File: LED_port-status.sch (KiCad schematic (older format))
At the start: 25 parts, among them P1 CONN_9

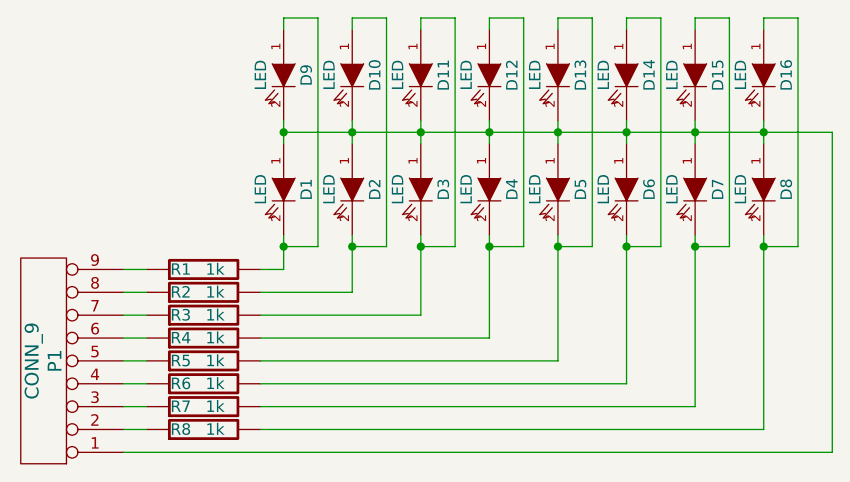
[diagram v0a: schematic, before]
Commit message: Switched to SMD resistor 4-packs.
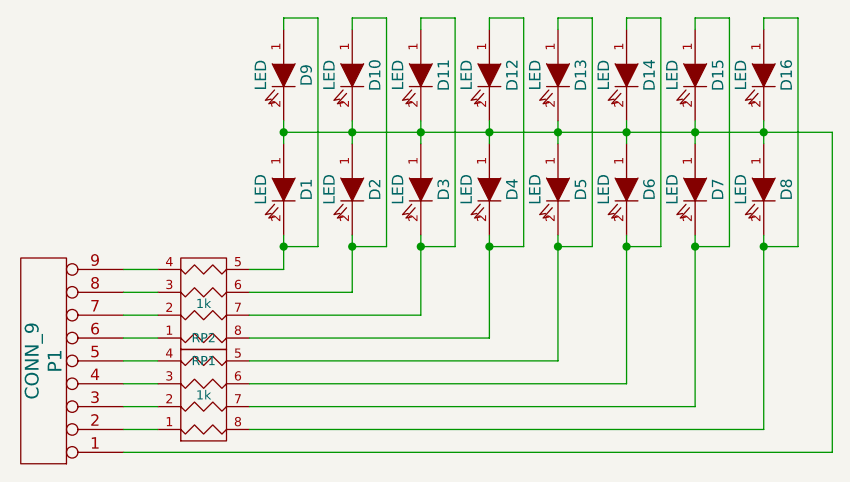
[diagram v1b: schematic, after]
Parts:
- removed R1, R2, R3, R4, R5, R6, R7, R8: 1k, symbol R
- added RP1, RP2: 1k, symbol R_PACK4
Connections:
- net at P1.2 (P2): now also RP2.1 (P1)
- net at P1.3 (P3): now also RP2.2 (P2)
- net at P1.4 (P4): now also RP2.3 (P3)
- net at P1.5 (P5): now also RP2.4 (P4)
- net at P1.6 (P6): now also RP1.1 (P1)
- net at P1.7 (P7): now also RP1.2 (P2)
- net at P1.8 (P8): now also RP1.3 (P3)
- net at P1.9 (P9): now also RP1.4 (P4)
- net at D1.2 (K), D9.1 (A): now also RP1.5 (R4)
- net at D10.1 (A), D2.2 (K): now also RP1.6 (R3)
- net at D11.1 (A), D3.2 (K): now also RP1.7 (R2)
- net at D12.1 (A), D4.2 (K): now also RP1.8 (R1)
- net at D13.1 (A), D5.2 (K): now also RP2.5 (R4)
- net at D14.1 (A), D6.2 (K): now also RP2.6 (R3)
- net at D15.1 (A), D7.2 (K): now also RP2.7 (R2)
- net at D16.1 (A), D8.2 (K): now also RP2.8 (R1)
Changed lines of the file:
@@
-EESchema Schematic File Version 2  date Mon 10 Dec 2012 09:48:04 PM CET
+EESchema Schematic File Version 2  date Sun 17 Feb 2013 02:52:17 PM CET
 LIBS:power
 LIBS:device
@@
 LIBS:contrib
 LIBS:valves
+LIBS:my_parts
 LIBS:LED_port-status-cache
 EELAYER 27 0
@@
 Sheet 1 1
 Title "LED_port-status"
-Date "10 dec 2012"
-Rev "0.10"
+Date "17 feb 2013"
+Rev "0.2"
 Comp "2012 - blog.spitzenpfeil.org"
 Comment1 ""
@@
 F 0 "P1" V 2150 3100 60  0000 C CNN
 F 1 "CONN_9" V 2250 3100 60  0000 C CNN
+F 2 "" H 2200 3100 60  0001 C CNN
+F 3 "" H 2200 3100 60  0001 C CNN
 	1    2200 3100
 	-1   0    0    1
-$EndComp
-$Comp
-L R R1
-U 1 1 50C62340
-P 2900 2700
-F 0 "R1" V 2900 2800 50  0000 C CNN
-F 1 "1k" V 2900 2650 50  0000 C CNN
-	1    2900 2700
-	0    -1   -1   0
-$EndComp
-$Comp
-L R R2
-U 1 1 50C62356
-P 2900 2800
-F 0 "R2" V 2900 2900 50  0000 C CNN
-F 1 "1k" V 2900 2750 50  0000 C CNN
-	1    2900 2800
-	0    -1   -1   0
-$EndComp
-$Comp
-L R R3
-U 1 1 50C62379
-P 2900 2900
-F 0 "R3" V 2900 3000 50  0000 C CNN
-F 1 "1k" V 2900 2850 50  0000 C CNN
-	1    2900 2900
-	0    -1   -1   0
-$EndComp
-$Comp
-L R R4
-U 1 1 50C62388
-P 2900 3000
-F 0 "R4" V 2900 3100 50  0000 C CNN
-F 1 "1k" V 2900 2950 50  0000 C CNN
-	1    2900 3000
-	0    -1   -1   0
-$EndComp
-$Comp
-L R R5
-U 1 1 50C623E7
-P 2900 3100
-F 0 "R5" V 2900 3200 50  0000 C CNN
-F 1 "1k" V 2900 3050 50  0000 C CNN
-	1    2900 3100
-	0    -1   -1   0
-$EndComp
-$Comp
-L R R6
-U 1 1 50C623F6
-P 2900 3200
-F 0 "R6" V 2900 3300 50  0000 C CNN
-F 1 "1k" V 2900 3150 50  0000 C CNN
-	1    2900 3200
-	0    -1   -1   0
-$EndComp
-$Comp
-L R R7
-U 1 1 50C62405
-P 2900 3300
-F 0 "R7" V 2900 3400 50  0000 C CNN
-F 1 "1k" V 2900 3250 50  0000 C CNN
-	1    2900 3300
-	0    -1   -1   0
-$EndComp
-$Comp
-L R R8
-U 1 1 50C62414
-P 2900 3400
-F 0 "R8" V 2900 3500 50  0000 C CNN
-F 1 "1k" V 2900 3350 50  0000 C CNN
-	1    2900 3400
-	0    -1   -1   0
 $EndComp
 $Comp
@@
 F 0 "D1" H 3250 2450 50  0000 C CNN
 F 1 "LED" H 3250 2250 50  0000 C CNN
+F 2 "" H 3250 2350 60  0001 C CNN
+F 3 "" H 3250 2350 60  0001 C CNN
 	1    3250 2350
 	0    1    1    0
@@
 F 0 "D3" H 3850 2450 50  0000 C CNN
 F 1 "LED" H 3850 2250 50  0000 C CNN
+F 2 "" H 3850 2350 60  0001 C CNN
+F 3 "" H 3850 2350 60  0001 C CNN
 	1    3850 2350
 	0    1    1    0
@@
 F 0 "D4" H 4150 2450 50  0000 C CNN
 F 1 "LED" H 4150 2250 50  0000 C CNN
+F 2 "" H 4150 2350 60  0001 C CNN
+F 3 "" H 4150 2350 60  0001 C CNN
 	1    4150 2350
 	0    1    1    0
@@
 F 0 "D5" H 4450 2450 50  0000 C CNN
 F 1 "LED" H 4450 2250 50  0000 C CNN
+F 2 "" H 4450 2350 60  0001 C CNN
+F 3 "" H 4450 2350 60  0001 C CNN
 	1    4450 2350
 	0    1    1    0
@@
 F 0 "D6" H 4750 2450 50  0000 C CNN
 F 1 "LED" H 4750 2250 50  0000 C CNN
+F 2 "" H 4750 2350 60  0001 C CNN
+F 3 "" H 4750 2350 60  0001 C CNN
 	1    4750 2350
 	0    1    1    0
@@
 F 0 "D7" H 5050 2450 50  0000 C CNN
 F 1 "LED" H 5050 2250 50  0000 C CNN
+F 2 "" H 5050 2350 60  0001 C CNN
+F 3 "" H 5050 2350 60  0001 C CNN
 	1    5050 2350
 	0    1    1    0
@@
 F 0 "D2" H 3550 2450 50  0000 C CNN
 F 1 "LED" H 3550 2250 50  0000 C CNN
+F 2 "" H 3550 2350 60  0001 C CNN
+F 3 "" H 3550 2350 60  0001 C CNN
 	1    3550 2350
 	0    1    1    0
@@
 F 0 "D8" H 5350 2450 50  0000 C CNN
 F 1 "LED" H 5350 2250 50  0000 C CNN
+F 2 "" H 5350 2350 60  0001 C CNN
+F 3 "" H 5350 2350 60  0001 C CNN
 	1    5350 2350
 	0    1    1    0
@@
 	5650 3500 2550 3500
 Wire Wire Line
-	3850 2900 3150 2900
-Wire Wire Line
-	3850 2550 3850 2900
+	3100 2900 3850 2900
+Wire Wire Line
+	3850 2900 3850 2550
 Wire Wire Line
 	4150 3000 4150 2550
 Wire Wire Line
-	3150 3000 4150 3000
-Wire Wire Line
-	4450 3100 3150 3100
-Wire Wire Line
-	4450 2550 4450 3100
+	3100 3000 4150 3000
+Wire Wire Line
+	3100 3100 4450 3100
+Wire Wire Line
+	4450 3100 4450 2550
 Wire Wire Line
 	4750 3200 4750 2550
 Wire Wire Line
-	3150 3200 4750 3200
-Wire Wire Line
-	5050 3300 3150 3300
-Wire Wire Line
-	5050 2550 5050 3300
+	3100 3200 4750 3200
+Wire Wire Line
+	3100 3300 5050 3300
+Wire Wire Line
+	5050 3300 5050 2550
 Wire Wire Line
 	5350 3400 5350 2550
 Wire Wire Line
-	3150 3400 5350 3400
+	3100 3400 5350 3400
 Wire Wire Line
 	3550 2800 3550 2550
 Wire Wire Line
-	3150 2800 3550 2800
+	3100 2800 3550 2800
 Wire Wire Line
 	3250 2700 3250 2550
 Wire Wire Line
-	3150 2700 3250 2700
+	3100 2700 3250 2700
 Wire Wire Line
 	3250 2100 5650 2100
 Wire Wire Line
-	2550 3400 2650 3400
-Wire Wire Line
-	2550 3300 2650 3300
-Wire Wire Line
-	2550 3200 2650 3200
-Wire Wire Line
-	2550 3100 2650 3100
-Wire Wire Line
-	2550 3000 2650 3000
-Wire Wire Line
-	2550 2900 2650 2900
-Wire Wire Line
-	2550 2800 2650 2800
-Wire Wire Line
-	2550 2700 2650 2700
+	2550 3400 2700 3400
+Wire Wire Line
+	2550 3300 2700 3300
+Wire Wire Line
+	2550 3200 2700 3200
+Wire Wire Line
+	2550 3100 2700 3100
+Wire Wire Line
+	2550 3000 2700 3000
+Wire Wire Line
+	2550 2900 2700 2900
+Wire Wire Line
+	2550 2800 2700 2800
+Wire Wire Line
+	2550 2700 2700 2700
 Wire Wire Line
 	5350 2050 5350 2150
@@
 F 0 "D9" H 3250 1950 50  0000 C CNN
 F 1 "LED" H 3250 1750 50  0000 C CNN
+F 2 "" H 3250 1850 60  0001 C CNN
+F 3 "" H 3250 1850 60  0001 C CNN
 	1    3250 1850
 	0    1    1    0
@@
 F 0 "D11" H 3850 1950 50  0000 C CNN
 F 1 "LED" H 3850 1750 50  0000 C CNN
+F 2 "" H 3850 1850 60  0001 C CNN
+F 3 "" H 3850 1850 60  0001 C CNN
 	1    3850 1850
 	0    1    1    0
@@
 F 0 "D12" H 4150 1950 50  0000 C CNN
 F 1 "LED" H 4150 1750 50  0000 C CNN
+F 2 "" H 4150 1850 60  0001 C CNN
+F 3 "" H 4150 1850 60  0001 C CNN
 	1    4150 1850
 	0    1    1    0
@@
 F 0 "D13" H 4450 1950 50  0000 C CNN
 F 1 "LED" H 4450 1750 50  0000 C CNN
+F 2 "" H 4450 1850 60  0001 C CNN
+F 3 "" H 4450 1850 60  0001 C CNN
 	1    4450 1850
 	0    1    1    0
@@
 F 0 "D14" H 4750 1950 50  0000 C CNN
 F 1 "LED" H 4750 1750 50  0000 C CNN
+F 2 "" H 4750 1850 60  0001 C CNN
+F 3 "" H 4750 1850 60  0001 C CNN
 	1    4750 1850
 	0    1    1    0
@@
 F 0 "D15" H 5050 1950 50  0000 C CNN
 F 1 "LED" H 5050 1750 50  0000 C CNN
+F 2 "" H 5050 1850 60  0001 C CNN
+F 3 "" H 5050 1850 60  0001 C CNN
 	1    5050 1850
 	0    1    1    0
@@
 F 0 "D10" H 3550 1950 50  0000 C CNN
 F 1 "LED" H 3550 1750 50  0000 C CNN
+F 2 "" H 3550 1850 60  0001 C CNN
+F 3 "" H 3550 1850 60  0001 C CNN
 	1    3550 1850
 	0    1    1    0
@@
 F 0 "D16" H 5350 1950 50  0000 C CNN
 F 1 "LED" H 5350 1750 50  0000 C CNN
+F 2 "" H 5350 1850 60  0001 C CNN
+F 3 "" H 5350 1850 60  0001 C CNN
 	1    5350 1850
 	0    1    1    0
@@
 	5350 1600 5350 1650
 Connection ~ 5350 2600
+$Comp
+L R_PACK4 RP1
+U 1 1 5120CCDC
+P 2900 2650
+F 0 "RP1" H 2900 3100 40  0000 C CNN
+F 1 "1k" H 2900 2850 40  0000 C CNN
+F 2 "" H 2900 2650 60  0000 C CNN
+F 3 "" H 2900 2650 60  0000 C CNN
+	1    2900 2650
+	1    0    0    1
+$EndComp
+$Comp
+L R_PACK4 RP2
+U 1 1 5120CD13
+P 2900 3050
+F 0 "RP2" H 2900 3000 40  0000 C CNN
+F 1 "1k" H 2900 3250 40  0000 C CNN
+F 2 "" H 2900 3050 60  0000 C CNN
+F 3 "" H 2900 3050 60  0000 C CNN
+	1    2900 3050
+	1    0    0    1
+$EndComp
 $EndSCHEMATC
